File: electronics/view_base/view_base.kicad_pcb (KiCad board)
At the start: 2 copper layers, 81.2 x 81.2 mm, 96 parts, among them J1 BLDC, J2 USB_C_Receptacle_USB2.0, J3 LCD, J4 A, J5 B, Q1 MMBT4403, Q2 UMH3N, U1 MT6701-CT, U2 T-Micro32_Plus, U3 CH340C, U4 HX711, U5 TMC6300, U6 AP1117-33, U7 SN74LV1T34DBV, U8 VEML7700

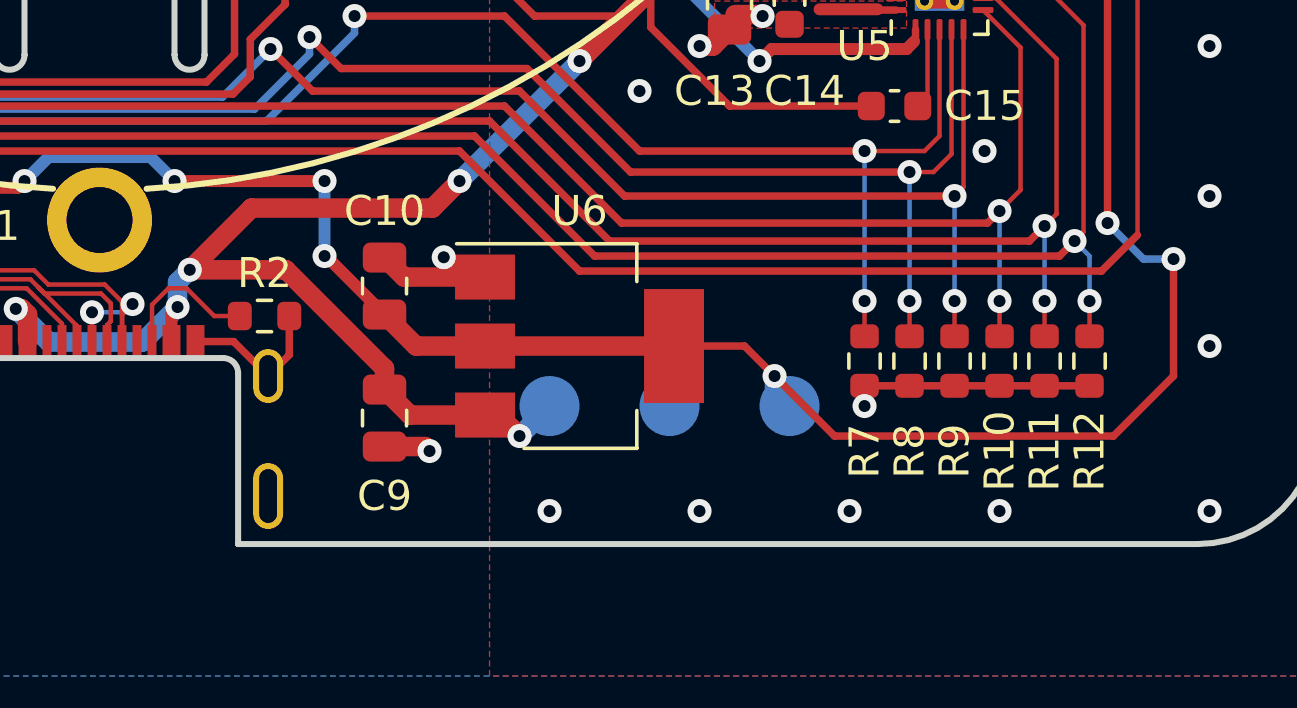
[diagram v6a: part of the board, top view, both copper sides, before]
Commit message: Fix HX711 analog supply, fix 3.3v regulator
Fixes #8
Fixes #3
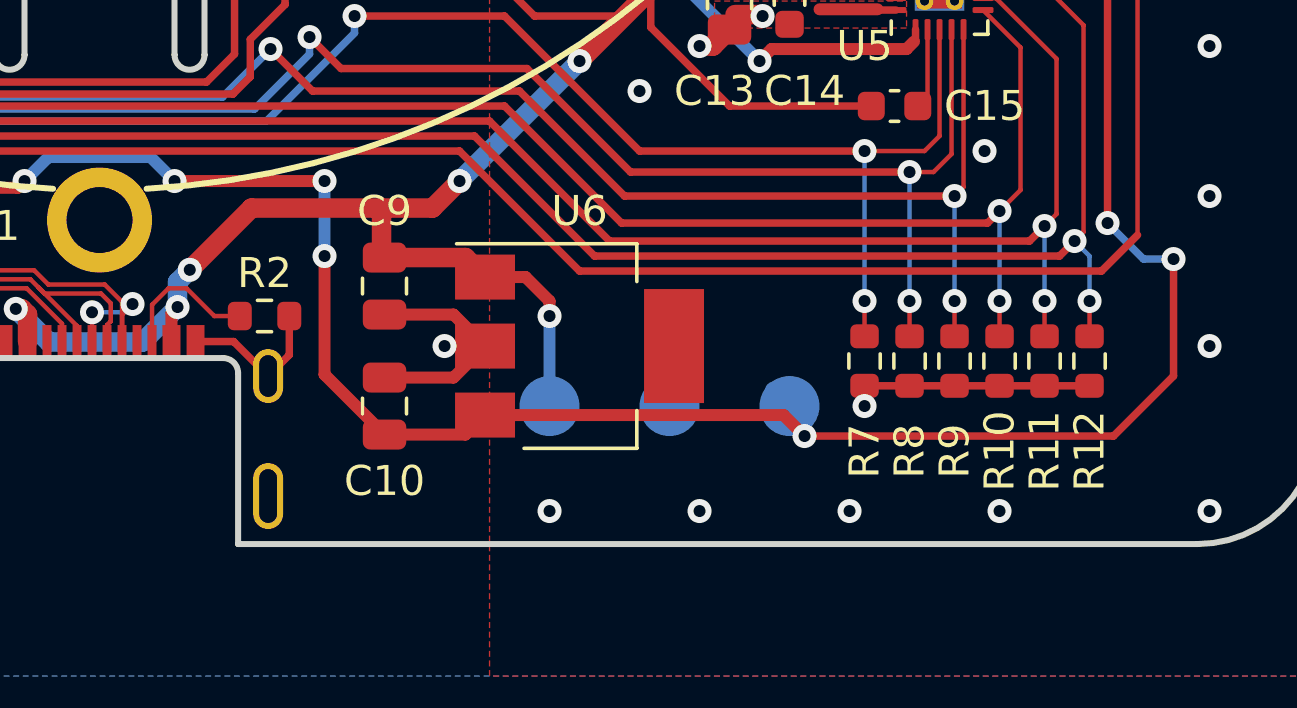
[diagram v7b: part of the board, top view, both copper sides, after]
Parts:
- R3: value 20k -> 10k
- U6: value AP1117-33 -> AP2114HA-3.3
- moved C9 4.40 mm to (109.5, 132.0)
- moved C10 4.00 mm to (109.5, 136.0)
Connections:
- U6 pad 1: GND -> +5V
- U6 pad 2: +3V3 -> GND
- U6 pad 3: +5V -> +3V3
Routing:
- net +3V3: track 308.9 -> 312.9 mm
- net +5V: track 255.1 -> 251.2 mm
- net GND: track 90.7 -> 92.8 mm, vias 86 -> 85

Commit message: Add a bunch of part numbers to BOM
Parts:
- H4, H5, H6, H7: footprint MountingHole:MountingHole_2.2mm_M2_ISO7380_Pad -> Holes:MountingHole_2.2mm_M2_ISO7380_Pad_NonVirtual
- Z1, Z2, Z3, Z4: value strain -> BF350-3AA Strain Gauge
